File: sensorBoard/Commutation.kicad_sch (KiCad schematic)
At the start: 18 parts, among them Q2 2N7002, U7 BTS50080-1TEA

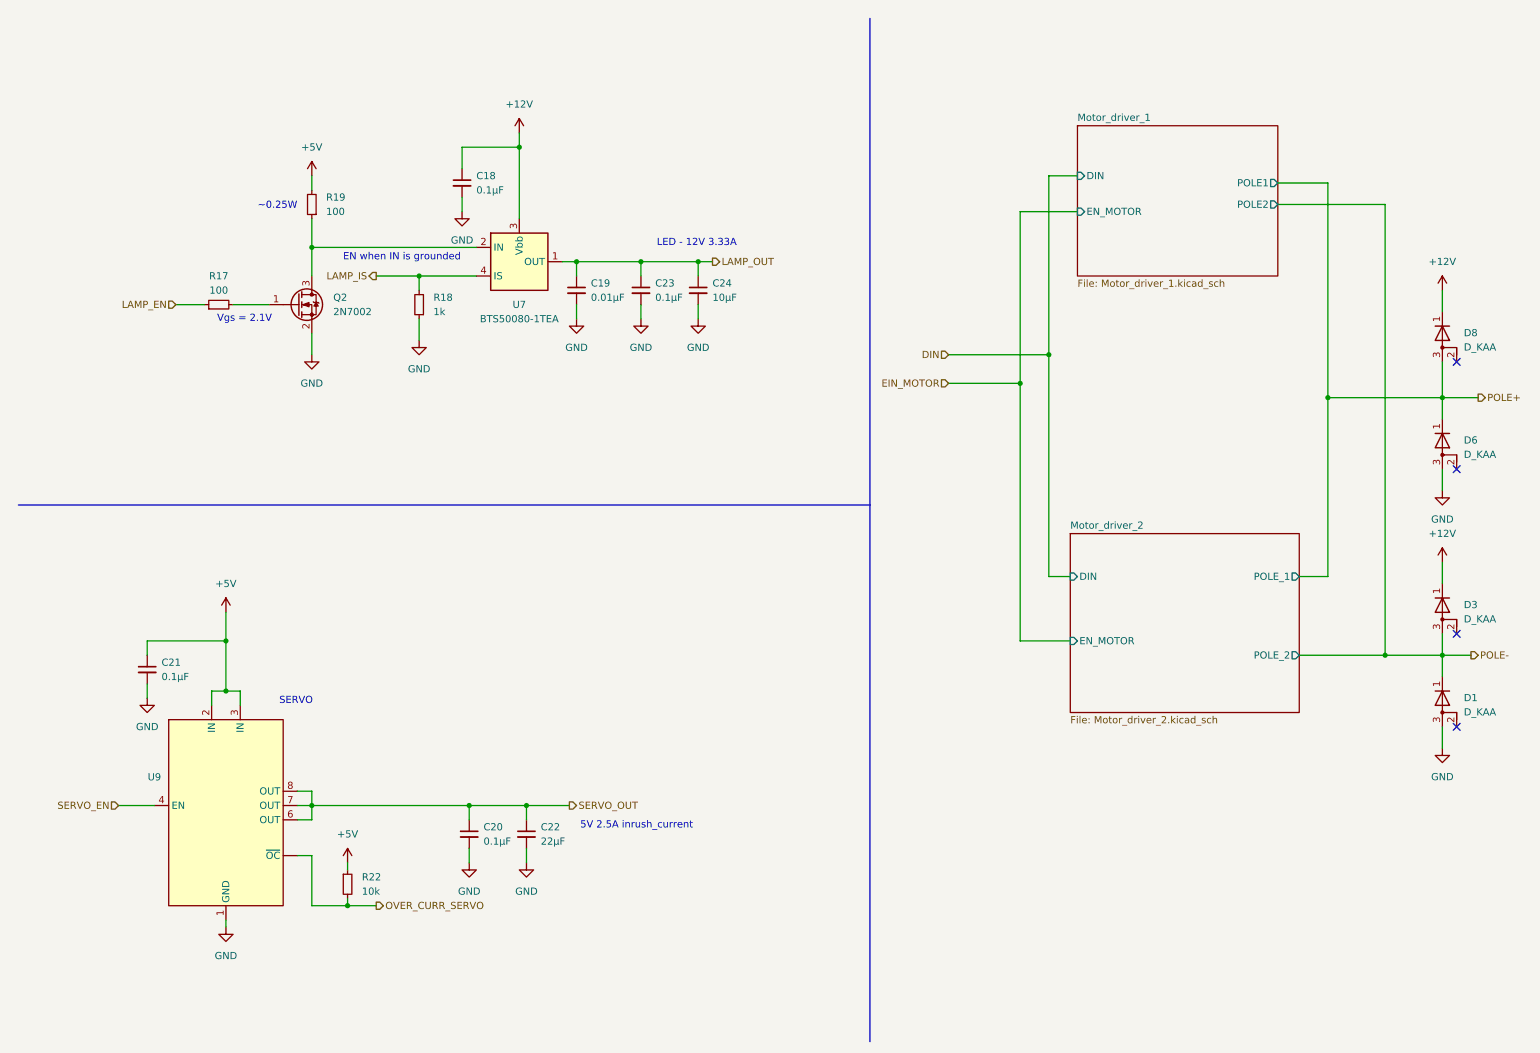
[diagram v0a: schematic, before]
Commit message: added the footprints, connectors left
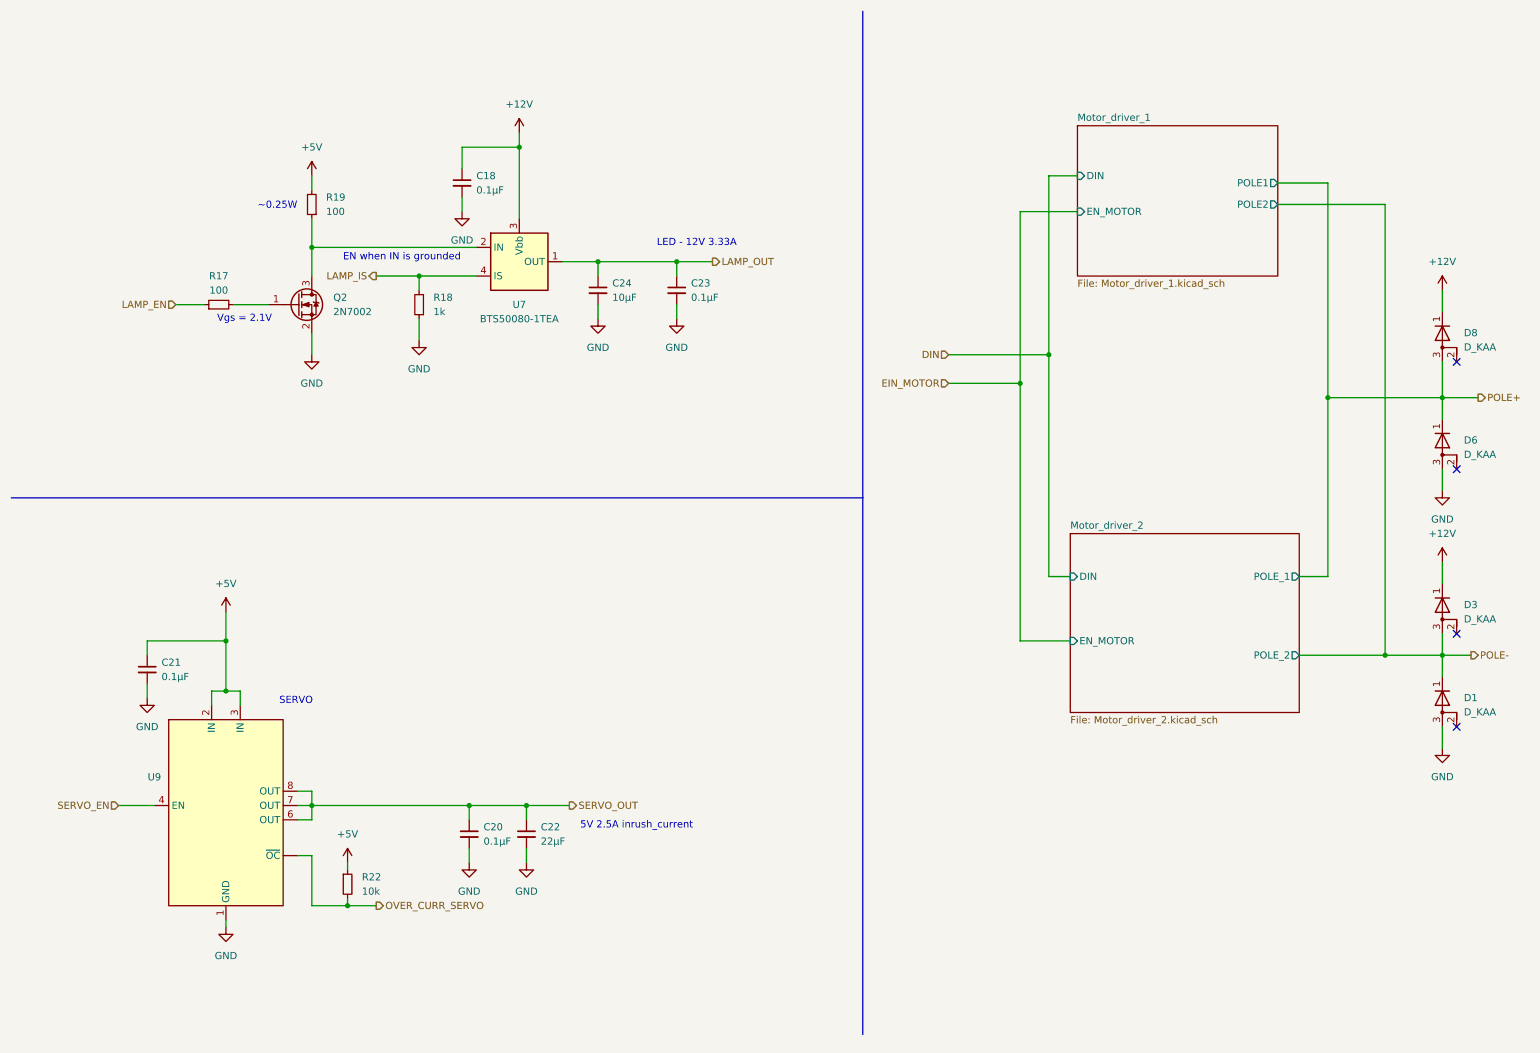
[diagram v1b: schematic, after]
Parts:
- removed C19: 0.01µF, symbol Device:C_Small
- C18: footprint (none) -> Capacitor_SMD:CP_Elec_18x17.5
- C20, C21, C22, C23, C24: footprint (none) -> Capacitor_SMD:C_0805_2012Metric
- D1, D3, D6, D8: footprint (none) -> Package_TO_SOT_SMD:TO-277A
- R17, R18, R19, R22: footprint (none) -> Resistor_SMD:R_0805_2012Metric
- U9: footprint (none) -> Package_SO:SOIC-8_3.9x4.9mm_P1.27mm
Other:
- moved on the sheet: C23, C24

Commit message: started the layout
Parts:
- removed C18: 0.1µF, Capacitor_SMD:CP_Elec_18x17.5, symbol Device:C_Small
- removed C23: 0.1µF, Capacitor_SMD:C_0805_2012Metric, symbol Device:C_Small
- removed C24: 10µF, Capacitor_SMD:C_0805_2012Metric, symbol Device:C_Small
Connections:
- net OVER_CURR_SERVO: now also U9.5 (~{OC}); no longer U9. (~{OC})

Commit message: started to connect layout. added 0 Ohm resistors to separate the drivers.
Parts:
- added R20, R21, R23, R24, R25, R30, R31, R32: 0, Resistor_SMD:R_0805_2012Metric, symbol Device:R_Small
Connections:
- net DIN: now also R21.2, R24.1
- net EIN_MOTOR: now also R20.2, R23.1
- net POLE+: now also R25.2, R31.1
- net POLE-: now also R30.2, R32.2
- new net Motor_driver_1/DIN: R21.1
- new net Motor_driver_1/EN_MOTOR: R20.1
- new net Motor_driver_1/POLE1: R25.1
- new net Motor_driver_1/POLE2: R30.1
- new net Motor_driver_2/DIN: R24.2
- new net Motor_driver_2/EN_MOTOR: R23.2
- new net Motor_driver_2/POLE_1: R31.2
- new net Motor_driver_2/POLE_2: R32.1
